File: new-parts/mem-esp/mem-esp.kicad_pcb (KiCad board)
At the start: 2 copper layers, 101.6 x 49.5 mm, 63 parts, among them J1 Conn_02x02_Odd_Even, J2 BHR-10-VUA, J3 BHR-10-VUA, J4 Conn_02x01, J5 Conn_02x01, J6 Conn_02x01, J7 Conn_02x01, U1 MC78M06_TO252, U2 ESP32-S3-DevKitC, U3 LTV-247, U4 LTV-247, U5 DRV8908, U6 LTV-247, U7 LTV-247, U8 LTV-247

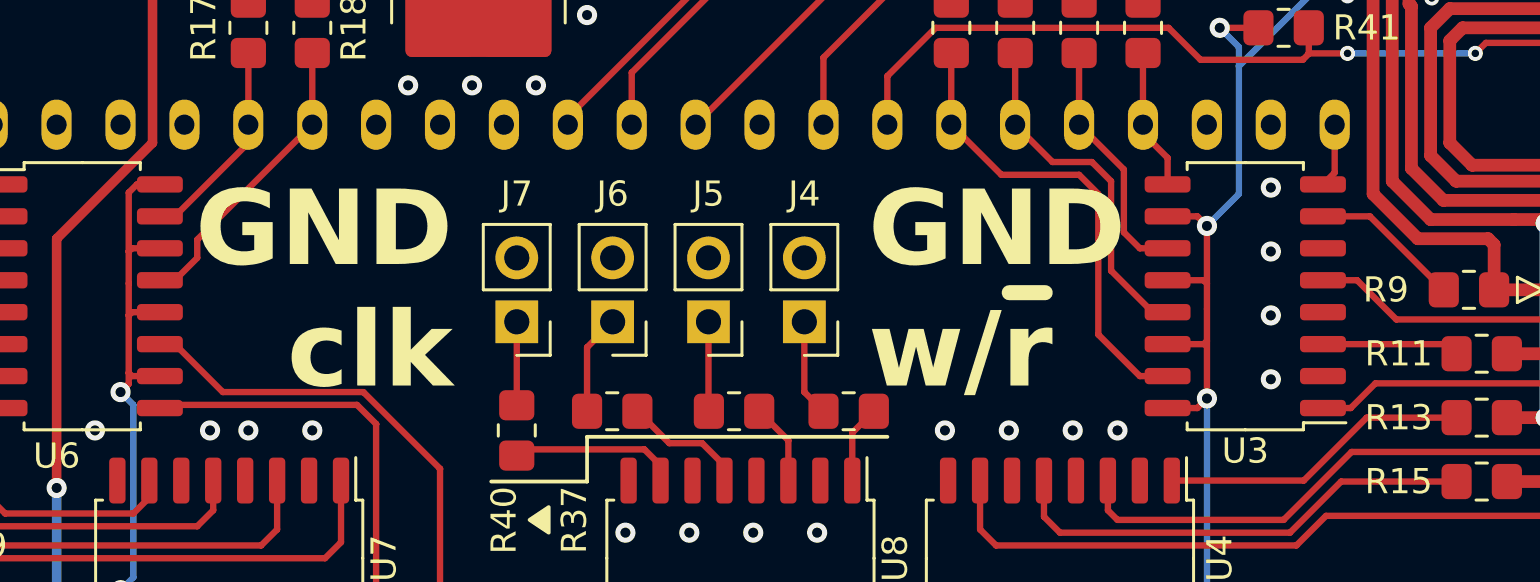
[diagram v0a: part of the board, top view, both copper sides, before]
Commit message: Change all two-pin headers for control + ground to control only.
This is to prevent accidental short circuits when they are plugged in the
wrong way.
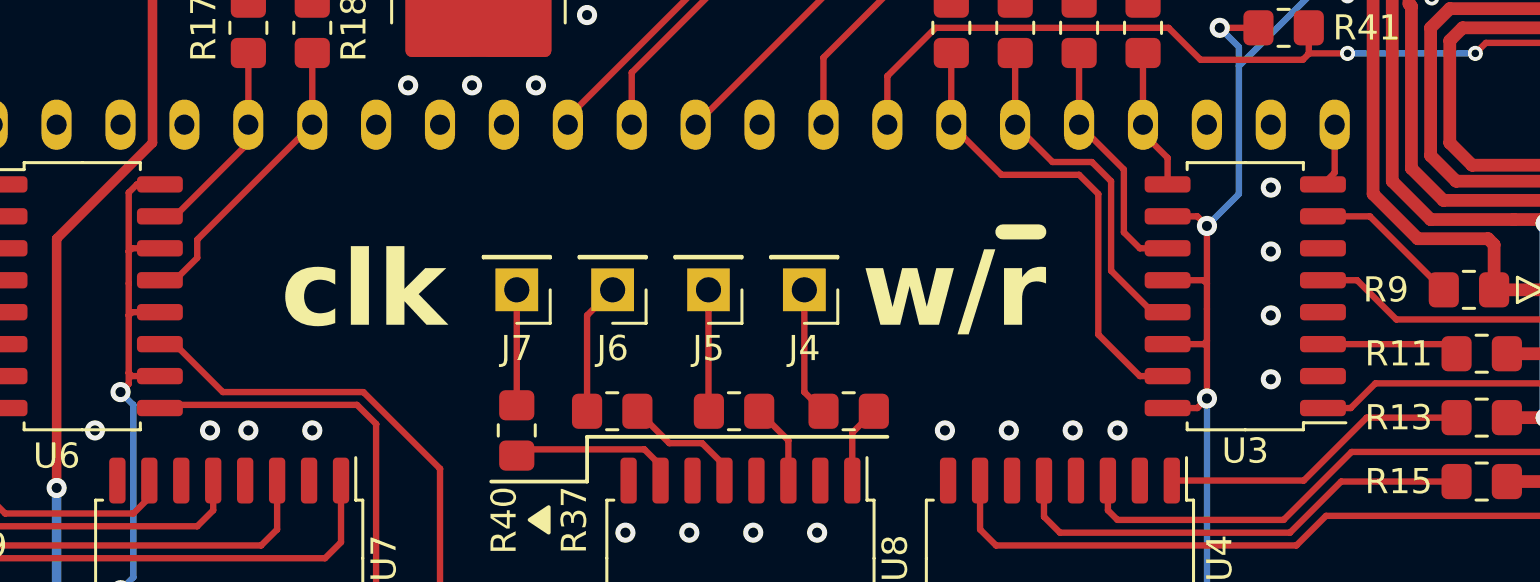
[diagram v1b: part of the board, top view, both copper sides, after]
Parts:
- J4, J5, J6, J7: footprint Connector_PinHeader_2.54mm:PinHeader_1x02_P2.54mm_Vertical -> Connector_PinHeader_2.54mm:PinHeader_1x01_P2.54mm_Vertical
- moved J4 1.27 mm to (160.0, 96.5)
- moved J5 1.27 mm to (156.2, 96.5)
- moved J6 1.27 mm to (152.4, 96.5)
- moved J7 1.27 mm to (148.6, 96.5)
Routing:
- net Net-(J7-Pin_1): track 3.32 -> 4.59 mm
- net Net-(J5-Pin_1): track 3.56 -> 4.83 mm
- net Net-(J4-Pin_1): track 3.87 -> 5.14 mm
- net Net-(J6-Pin_1): track 3.98 -> 5.25 mm
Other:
- board text added: "clk"
- board text added: "w/~{r}"
- board text removed: "GND clk"
- board text removed: "GND w/~{r}"

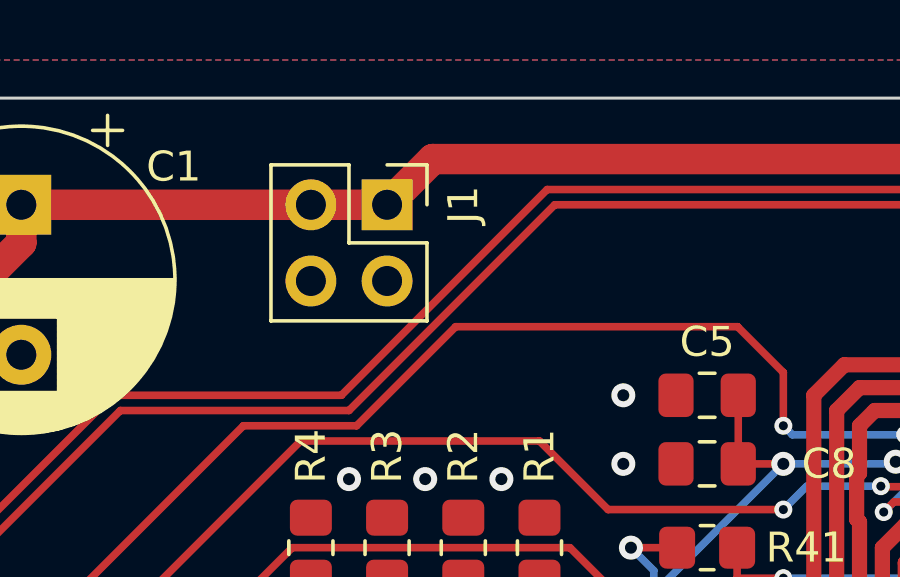
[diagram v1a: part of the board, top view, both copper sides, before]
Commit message: mem-esp: Label power supply header.
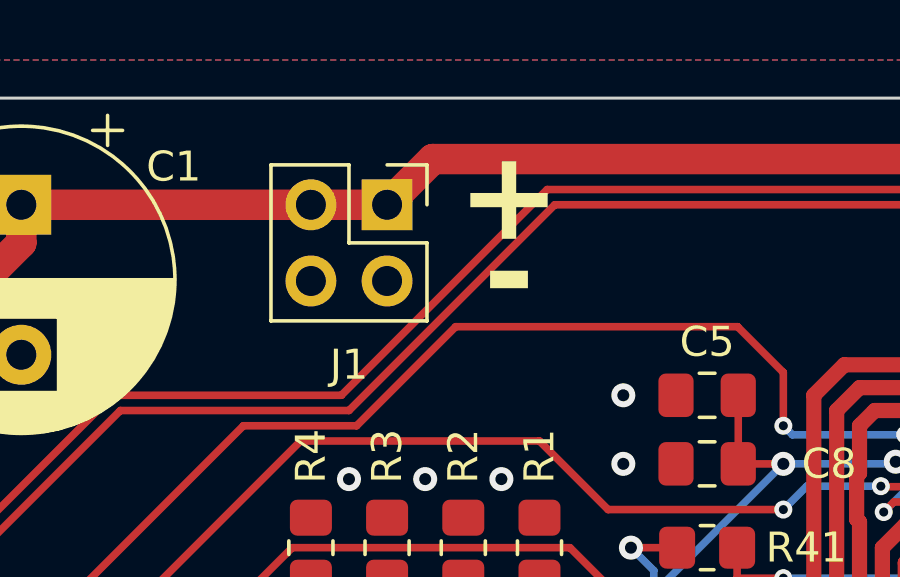
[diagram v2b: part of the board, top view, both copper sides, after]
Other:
- board text added: "+"
- board text added: "-"
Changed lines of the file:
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@@
     (property "ki_keywords" "connector")
     (attr through_hole)
-    (fp_text reference "J1" (at 0 -2.54 90) (layer "F.SilkS")
+    (fp_text reference "J1" (at 5.334 1.27 -180) (layer "F.SilkS")
         (effects (font (size 1 1) (thickness 0.15)))
     )
@@
     (effects (font (size 3 3) (thickness 0.6) bold))
   )
+  (gr_text "-" (at 172.466 76.962) (layer "F.SilkS")
+    (effects (font (size 3 3) (thickness 0.6) bold))
+  )
+  (gr_text "+" (at 172.466 74.422) (layer "F.SilkS")
+    (effects (font (size 3 3) (thickness 0.6) bold))
+  )

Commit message: Add placeholders for JLC order number.
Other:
- board text added: "JLCJLCJLCJLC"
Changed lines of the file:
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@@
   (gr_line (start 210.82 71.12) (end 210.82 120.65)
     (stroke (width 0.1) (type default)) (layer "Edge.Cuts"))
+  (gr_text "JLCJLCJLCJLC" (at 209.296 119.126) (layer "B.SilkS")
+    (effects (font (size 1 1) (thickness 0.15)) (justify left bottom mirror))
+  )
   (gr_text "addr in" (at 119.38 86.36) (layer "F.SilkS")
     (effects (font (size 3 3) (thickness 0.6) bold))

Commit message: Add a "title" label to all parts.
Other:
- board text added: "memory controller"
- board text added: "vis vitalis"
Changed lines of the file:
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@@
   (gr_line (start 210.82 71.12) (end 210.82 120.65)
     (stroke (width 0.1) (type default)) (layer "Edge.Cuts"))
+  (gr_text "memory controller\n" (at 110.744 76.454) (layer "B.SilkS")
+    (effects (font (size 3 3) (thickness 0.6) bold) (justify right bottom mirror))
+  )
+  (gr_text "vis vitalis" (at 170.688 76.454) (layer "B.SilkS")
+    (effects (font (size 3 3) (thickness 0.6) bold) (justify right bottom mirror))
+  )
   (gr_text "JLCJLCJLCJLC" (at 209.296 119.126) (layer "B.SilkS")
     (effects (font (size 1 1) (thickness 0.15)) (justify left bottom mirror))

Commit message: Fix connector values: change names from 2 rows to 1 row.
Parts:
- J4, J5, J6, J7: value Conn_02x01 -> Conn_01x01
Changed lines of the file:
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@@
         (effects (font (size 1 1) (thickness 0.15)))
     )
-    (fp_text value "Conn_02x01" (at 0 2.33 180) (layer "F.Fab")
+    (fp_text value "Conn_01x01" (at 0 2.33 180) (layer "F.Fab")
         (effects (font (size 1 1) (thickness 0.15)))
     )
@@
         (effects (font (size 1 1) (thickness 0.15)))
     )
-    (fp_text value "Conn_02x01" (at 0 2.33 180) (layer "F.Fab")
+    (fp_text value "Conn_01x01" (at 0 2.33 180) (layer "F.Fab")
         (effects (font (size 1 1) (thickness 0.15)))
     )
@@
         (effects (font (size 1 1) (thickness 0.15)))
     )
-    (fp_text value "Conn_02x01" (at 0 2.33 180) (layer "F.Fab")
+    (fp_text value "Conn_01x01" (at 0 2.33 180) (layer "F.Fab")
         (effects (font (size 1 1) (thickness 0.15)))
     )
@@
         (effects (font (size 1 1) (thickness 0.15)))
     )
-    (fp_text value "Conn_02x01" (at 0 2.33 180) (layer "F.Fab")
-        (effects (font (size 1 1) (thickness 0.15)))
-    )
+    (fp_text value "Conn_01x01" (at 0 2.33 180) (layer "F.Fab")
+        (effects (font (size 1 1) (thickness 0.15)))
+    )

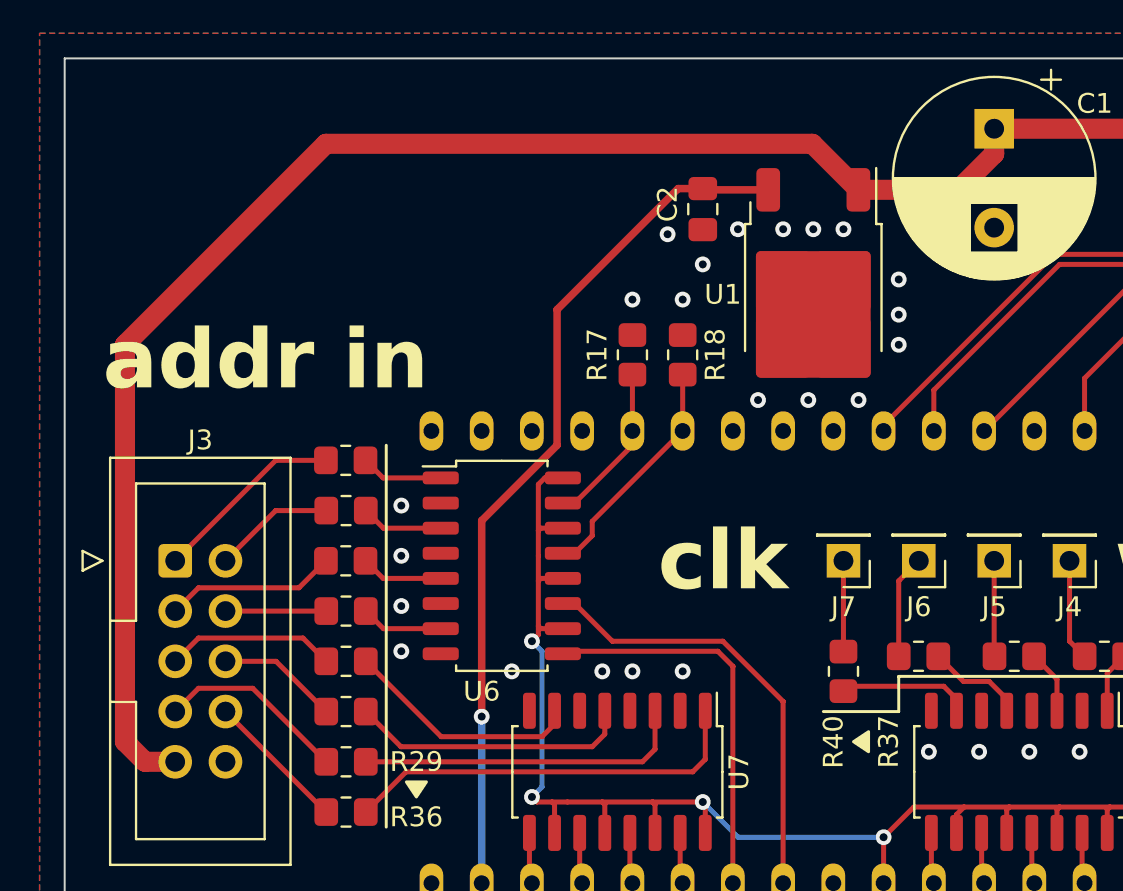
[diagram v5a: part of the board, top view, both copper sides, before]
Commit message: mem-esp: Change to a THT power regulator for better heat dissipation.
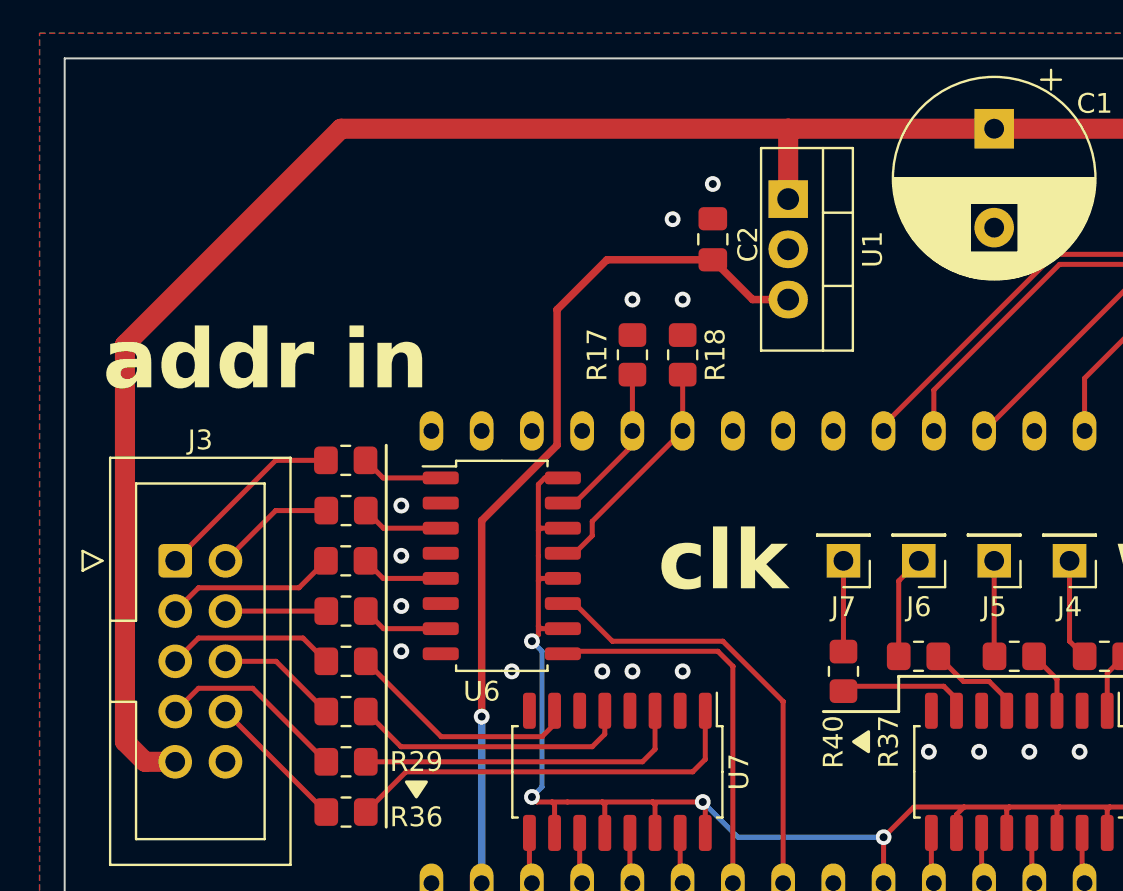
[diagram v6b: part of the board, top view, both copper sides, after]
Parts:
- U1: value MC78M06_TO252 -> LM7806_TO220; footprint Package_TO_SOT_SMD:TO-252-2 -> Package_TO_SOT_THT:TO-220-3_Vertical
- moved U1 4.75 mm to (145.8, 78.2)
- moved C2 1.61 mm to (142.0, 80.3), turned to 90 degrees
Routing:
- net +12V: track 184.3 -> 185.2 mm
- net GND: vias 63 -> 53
